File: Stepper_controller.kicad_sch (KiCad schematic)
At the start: 30 parts, among them J6 Encoder connector, J7 Motor connector, U3 TMC5130A-TA

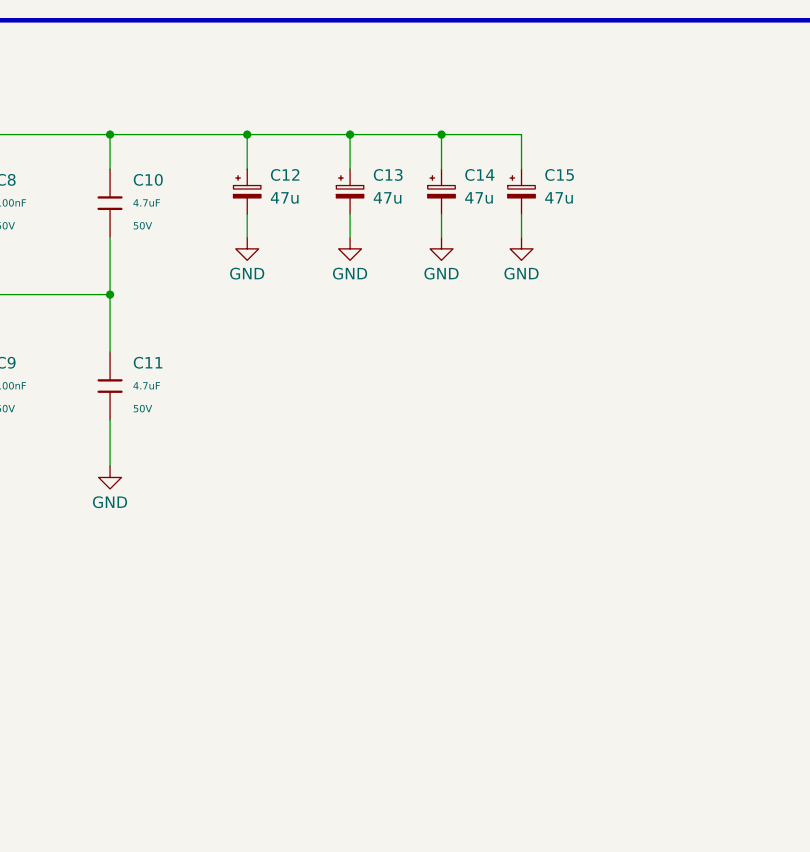
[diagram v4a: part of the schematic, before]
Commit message: Added design rules to PCB and updated dip switch
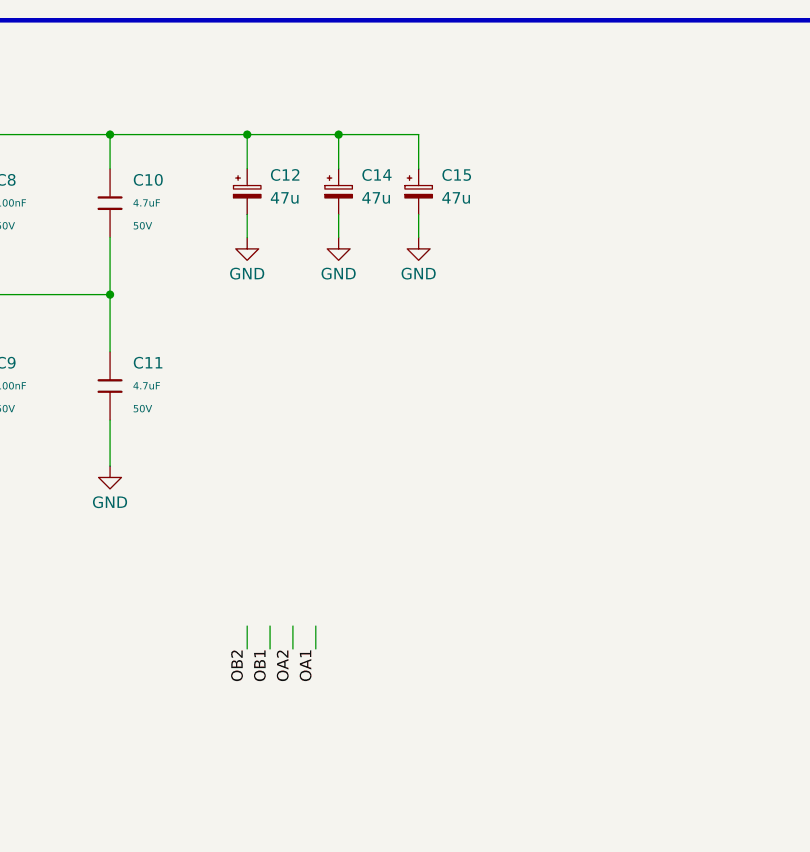
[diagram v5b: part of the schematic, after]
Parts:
- removed C13: 47u, Capacitor_SMD:CP_Elec_6.3x7.7, symbol Device:C_Polarized_Small
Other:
- moved on the sheet: C14, C15

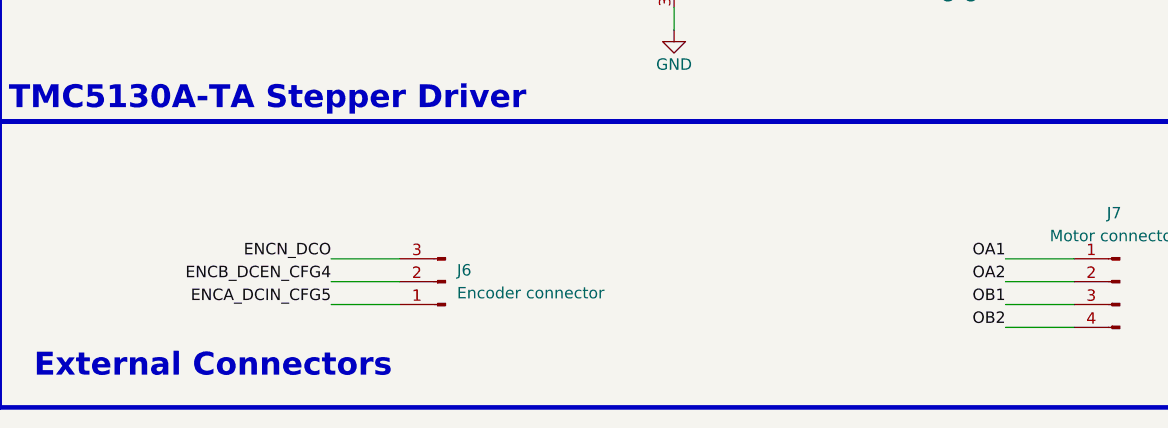
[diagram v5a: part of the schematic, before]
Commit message: Added Routing
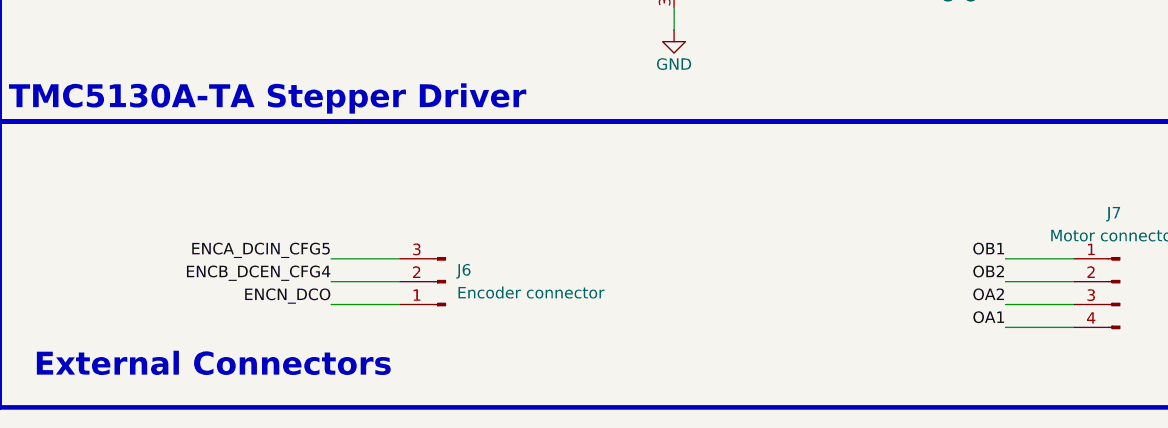
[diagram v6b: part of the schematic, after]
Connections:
- net ENCA_DCIN_CFG5: now also J6.3 (Pin_3); no longer J6.1 (Pin_1)
- net ENCN_DCO: now also J6.1 (Pin_1); no longer J6.3 (Pin_3)
- net OA1: now also J7.4 (Pin_4); no longer J7.1 (Pin_1)
- net OA2: now also J7.3 (Pin_3); no longer J7.2 (Pin_2)
- net OB1: now also J7.1 (Pin_1); no longer J7.3 (Pin_3)
- net OB2: now also J7.2 (Pin_2); no longer J7.4 (Pin_4)

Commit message: updated routing
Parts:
- added JP1, JP2, JP3: SolderJumper_2_Open, Jumper:SolderJumper-2_P1.3mm_Open_TrianglePad1.0x1.5mm, symbol Jumper:SolderJumper_2_Open
- added TP7: TestPoint, TestPoint:TestPoint_Pad_D1.0mm, symbol Connector:TestPoint
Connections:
- net U_reg: now also JP1.1 (A), JP2.1 (A), JP3.1 (A); no longer C10.1, C12.1, C14.1, C15.1, C7.1, C8.1, D3.2, R8.1, U3.21 (VS), U3.39 (VSA), U3.40 (VS)
- new net U_reg_after_jumper: C10.1, C12.1, C14.1, C15.1, C7.1, C8.1, D3.2, JP1.2 (B), JP2.2 (B), JP3.2 (B), R8.1, TP7.1, U3.21 (VS), U3.39 (VSA), U3.40 (VS)

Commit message: minor fixes + production files
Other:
- title: (none) -> MMS3 Stepper Controler
- moved on the sheet: C3, TP7
